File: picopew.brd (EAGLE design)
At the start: 48.4 x 20 mm, 73 parts, among them U1 IS31FL3733-TQLS4

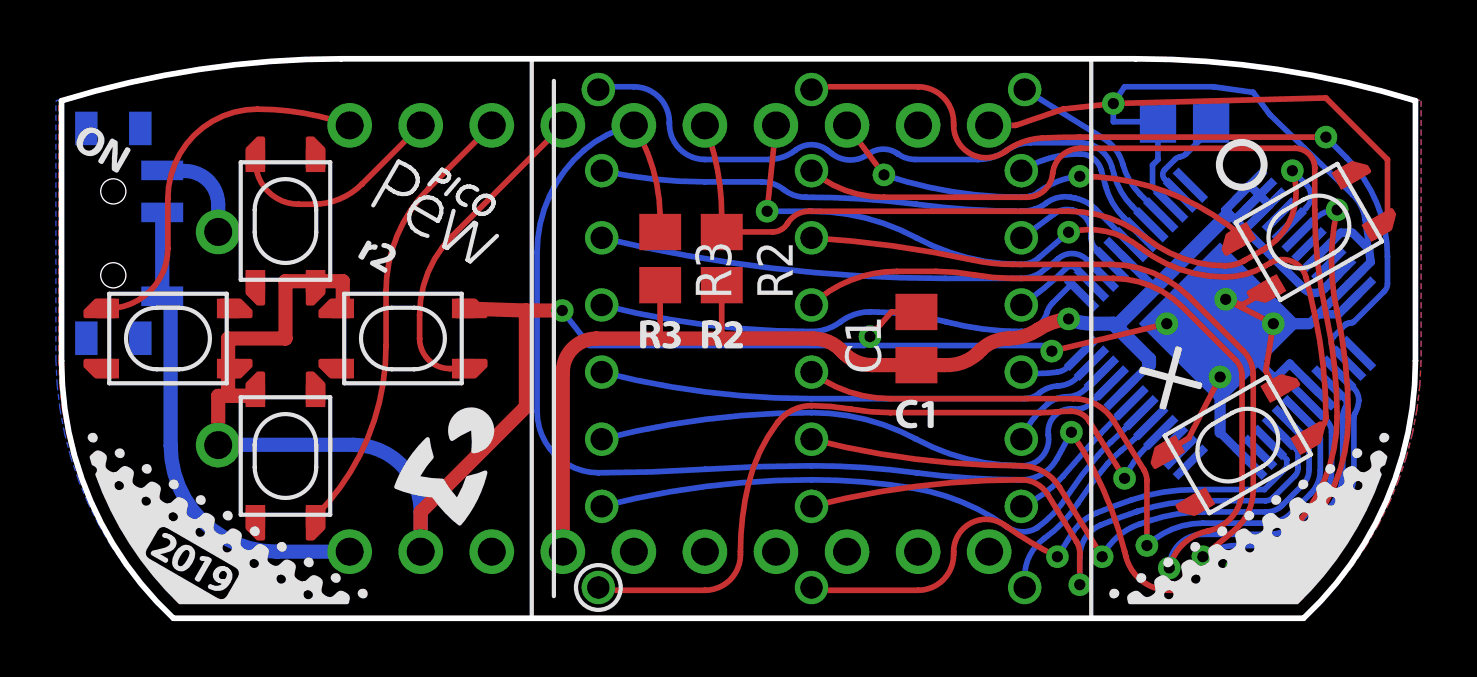
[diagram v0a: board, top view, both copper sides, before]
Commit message: Add JST connector footprint for those who want to connect their battery that way.
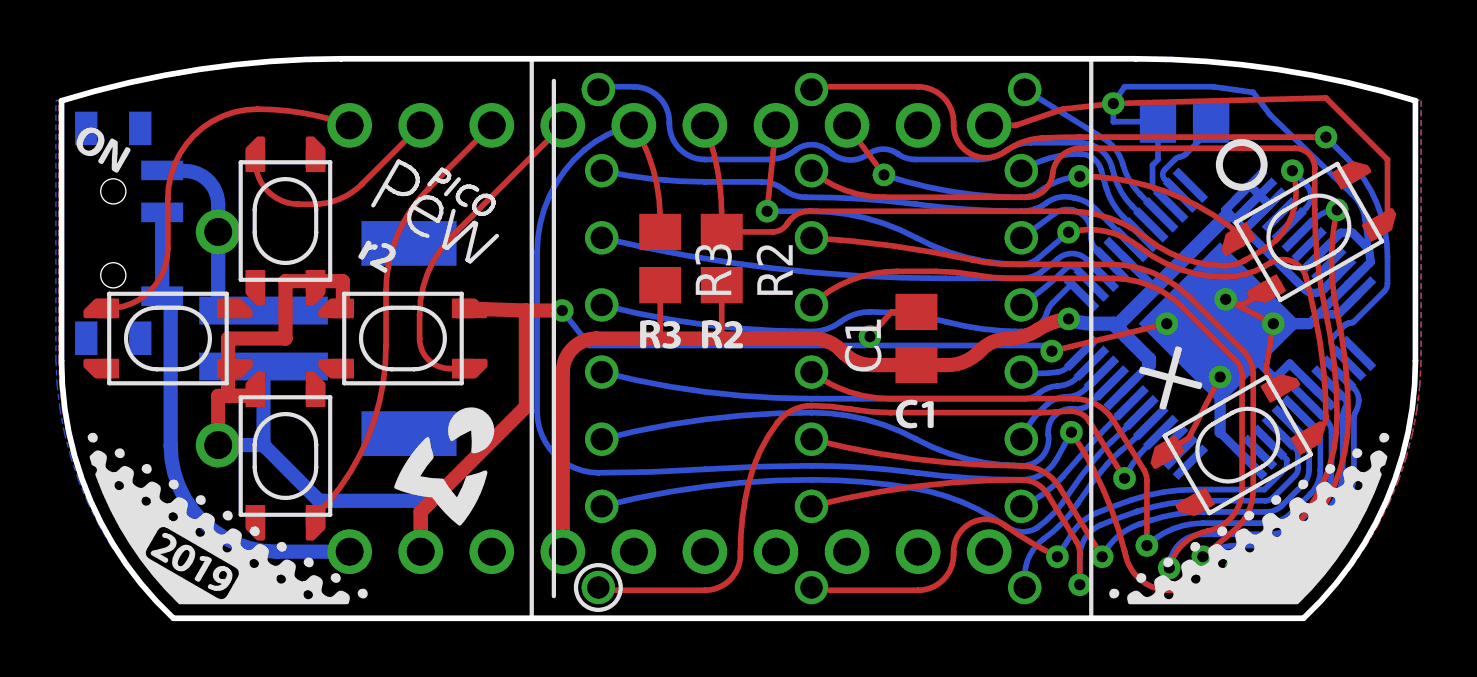
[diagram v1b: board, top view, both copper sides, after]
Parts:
- added CN1: (no value), cwpackage:JST-PH-2-SMT-RA
- moved U$12 1.28 mm to (7.00, 7.40)
- moved U$4 1.28 mm to (7.00, 12.6)
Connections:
- net GND: now also CN1.2
- net N$31: now also CN1.1
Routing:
- net N$31: track 2.88 -> 7.91 mm
- net GND: track 138.5 -> 141.6 mm
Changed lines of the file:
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@@
 <element name="U$30" library="cwtypeset" package="CHAR054" value="" x="20" y="6.857" rot="MR270"/>
 <element name="U$31" library="cwtypeset" package="CHAR057" value="" x="20" y="6.092" rot="MR270"/>
-<element name="U$4" library="cwlogo" package="PLUS" value="" x="8" y="11.8" rot="MR270"/>
-<element name="U$12" library="cwlogo" package="MINUS" value="" x="8" y="8.2" rot="MR270"/>
+<element name="U$4" library="cwlogo" package="PLUS" value="" x="7" y="12.6" rot="MR270"/>
+<element name="U$12" library="cwlogo" package="MINUS" value="" x="7" y="7.4" rot="MR270"/>
+<element name="CN1" library="cwpackage" package="JST-PH-2-SMT-RA" value="" x="13.32" y="10" rot="MR90"/>
 </elements>
 <signals>
@@
 <wire x1="47.6" y1="18.6" x2="49.8" y2="16.4" width="0.2032" layer="1"/>
 <wire x1="49.8" y1="16.4" x2="49.8" y2="14.36456875" width="0.2032" layer="1"/>
-<wire x1="15.24" y1="2.38" x2="15.24" y2="3.8" width="0.508" layer="16"/>
-<wire x1="15.24" y1="3.8" x2="12.84" y2="6.2" width="0.508" layer="16" curve="90"/>
-<wire x1="8" y1="6.2" x2="12.84" y2="6.2" width="0.508" layer="16"/>
+<wire x1="15.24" y1="2.38" x2="15.24" y2="4.2" width="0.508" layer="16"/>
 <wire x1="41.595" y1="17.75" x2="40" y2="17.75" width="0.2032" layer="16"/>
 <wire x1="40" y1="17.75" x2="40" y2="18.4" width="0.2032" layer="16"/>
@@
 <wire x1="48.125940625" y1="13.780278125" x2="48.550203125" y2="13.780278125" width="0.3048" layer="16"/>
 <wire x1="48.550203125" y1="13.780278125" x2="49.138675" y2="13.191803125" width="0.3048" layer="16"/>
+<contactref element="CN1" pad="2"/>
+<wire x1="9.62" y1="9" x2="9.62" y2="6.19" width="0.508" layer="16"/>
+<wire x1="9.62" y1="6.19" x2="8" y2="6.19" width="0.508" layer="16"/>
+<wire x1="15.24" y1="4.2" x2="11.6" y2="4.2" width="0.508" layer="16"/>
+<wire x1="11.6" y1="4.2" x2="9.62" y2="6.19" width="0.508" layer="16"/>
 </signal>
 <signal name="N$1">
@@
 <wire x1="6.8" y1="15.99" x2="8" y2="14.79" width="0.508" layer="16" curve="-90"/>
 <wire x1="8" y1="14.79" x2="8" y2="13.81" width="0.508" layer="16"/>
-<wire x1="6.6" y1="15.99" x2="6" y2="16.01" width="0" layer="19" extent="16-16"/>
+<contactref element="CN1" pad="1"/>
+<wire x1="8" y1="13.81" x2="8" y2="11" width="0.508" layer="16"/>
+<wire x1="8" y1="11" x2="9.62" y2="11" width="0.508" layer="16"/>
+<wire x1="6.6" y1="15.99" x2="6" y2="16.01" width="0.508" layer="16"/>
 </signal>
 <signal name="N$33">

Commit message: Move R2 and R3 to be more centered under the LED matrix.
Hoping this reduces the likelihood that the resistors will prevent the matrix from sitting flush on the board.
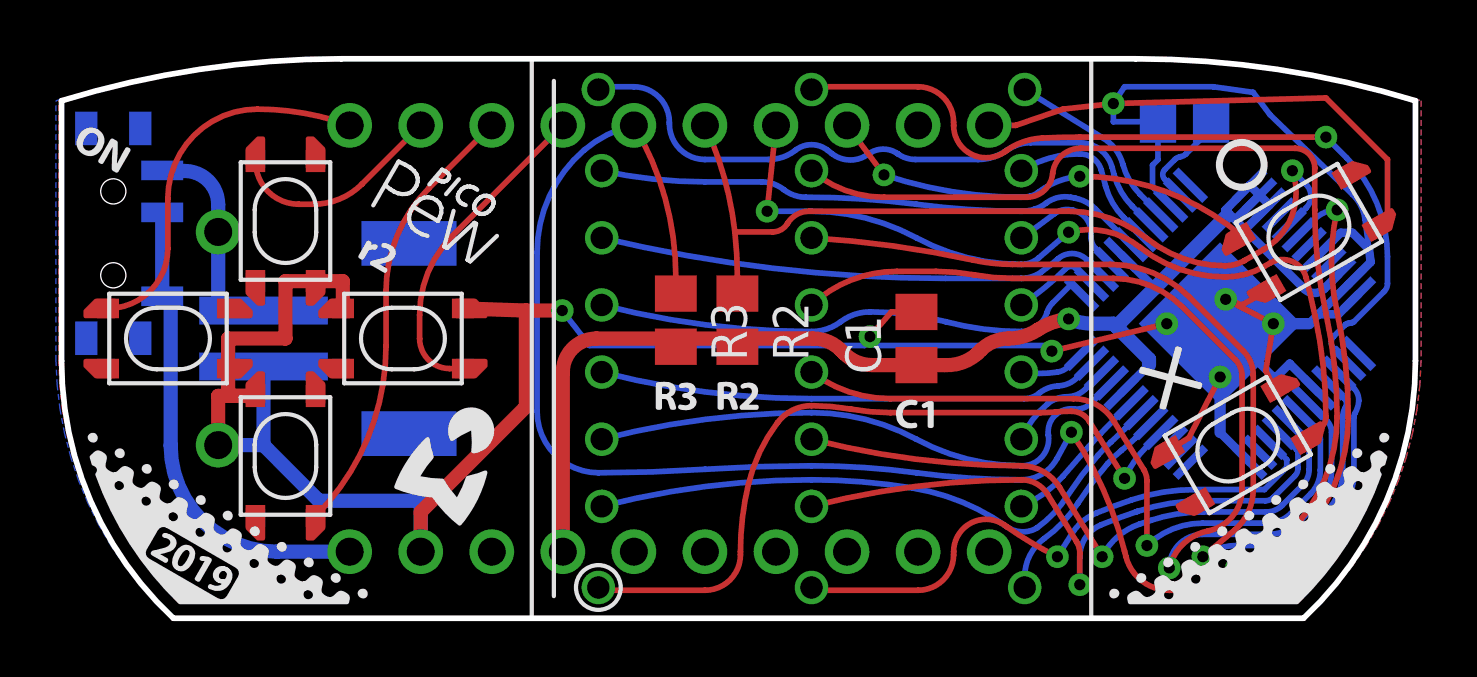
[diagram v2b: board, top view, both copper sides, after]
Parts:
- moved U$20 2.27 mm to (25.8, 7.45)
- moved U$21 2.27 mm to (26.6, 7.45)
- moved U$22 2.27 mm to (23.6, 7.45)
- moved U$23 2.27 mm to (24.4, 7.45)
- moved R2 2.27 mm to (26.6, 10.7)
- moved R3 2.27 mm to (24.4, 10.7)
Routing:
- net +3V3: track 52.0 -> 48.8 mm
- net N$26: track 62.3 -> 64.6 mm
- net N$25: track 29.3 -> 31.1 mm
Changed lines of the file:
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@@
 <element name="X" library="cwpackage" package="MICROPUSHBUTTON" value="PTS815" x="44.45" y="6.19" rot="R30"/>
 <element name="R1" library="resistor" package="R0805" value="22K" x="42.545" y="17.75" rot="MR180"/>
-<element name="R2" library="resistor" package="R0805" value="4.7K" x="26" y="12.8575" rot="R270"/>
-<element name="R3" library="resistor" package="R0805" value="4.7K" x="23.8" y="12.8575" rot="R270"/>
+<element name="R2" library="resistor" package="R0805" value="4.7K" x="26.56" y="10.6575" rot="R270"/>
+<element name="R3" library="resistor" package="R0805" value="4.7K" x="24.36" y="10.6575" rot="R270"/>
 <element name="C1" library="resistor" package="C0805" value="1µ" x="32.96" y="10" rot="R90"/>
 <element name="3" library="cwpackage" package="MICROSLIDESWITCH" value="PCM12SMTR" x="4.25" y="13.76" rot="MR90"/>
@@
 <element name="U$14" library="cwtypeset" package="CHAR082" value="" x="45.75" y="18.45" rot="MR270"/>
 <element name="U$19" library="cwtypeset" package="CHAR049" value="" x="45.75" y="17.625" rot="MR270"/>
-<element name="U$20" library="cwtypeset" package="CHAR082" value="" x="25.24" y="9.65"/>
-<element name="U$21" library="cwtypeset" package="CHAR050" value="" x="26.065" y="9.65"/>
-<element name="U$22" library="cwtypeset" package="CHAR082" value="" x="23.03" y="9.65"/>
-<element name="U$23" library="cwtypeset" package="CHAR051" value="" x="23.855" y="9.65"/>
+<element name="U$20" library="cwtypeset" package="CHAR082" value="" x="25.8" y="7.45"/>
+<element name="U$21" library="cwtypeset" package="CHAR050" value="" x="26.625" y="7.45"/>
+<element name="U$22" library="cwtypeset" package="CHAR082" value="" x="23.59" y="7.45"/>
+<element name="U$23" library="cwtypeset" package="CHAR051" value="" x="24.415" y="7.45"/>
 <element name="U$24" library="cwtypeset" package="CHAR067" value="" x="32.22" y="6.8"/>
 <element name="U$25" library="cwtypeset" package="CHAR049" value="" x="33.059" y="6.8"/>
@@
 <wire x1="28.35189375" y1="14.1135125" x2="29.121775" y2="14.55" width="0.2032" layer="1" curve="-59.102503"/>
 <wire x1="29.121775" y1="14.55" x2="38.4" y2="14.55" width="0.2032" layer="1"/>
-<wire x1="26.0375" y1="13.81" x2="27.816553125" y2="13.81" width="0.2032" layer="1"/>
-<wire x1="27.816553125" y1="13.81" x2="28.35189375" y2="14.1135125" width="0.2032" layer="1" curve="59.102542"/>
-<wire x1="26.0375" y1="13.81" x2="26" y2="13.8075" width="0.2032" layer="1"/>
 <wire x1="44" y1="12.6" x2="44.675209375" y2="12.780921875" width="0.2032" layer="1" curve="29.999803"/>
 <wire x1="44.675209375" y1="12.780921875" x2="44.68268125" y2="12.785234375" width="0.2032" layer="1"/>
-<wire x1="26" y1="13.8075" x2="26" y2="14.4" width="0.2032" layer="1"/>
-<wire x1="26" y1="14.4" x2="25.4" y2="17.62" width="0.2032" layer="1" curve="21.11036"/>
 <wire x1="44.68268125" y1="12.785234375" x2="45.353453125" y2="13.172503125" width="0.2032" layer="1"/>
 <wire x1="45.353453125" y1="13.172503125" x2="46.4" y2="16" width="0.2032" layer="1" curve="79.378049"/>
 <wire x1="38.4" y1="14.55" x2="41.2" y2="13.575" width="0.2032" layer="1" curve="-38.397747"/>
 <wire x1="41.2" y1="13.575" x2="44" y2="12.6" width="0.2032" layer="1" curve="38.39785"/>
+<wire x1="26.56" y1="11.6075" x2="26.56" y2="12.2" width="0.2032" layer="1"/>
+<wire x1="27.816553125" y1="13.81" x2="28.35189375" y2="14.1135125" width="0.2032" layer="1" curve="59.102542"/>
+<wire x1="26.56" y1="12.2" x2="26.47" y2="13.81" width="0.2032" layer="1" curve="6.399079"/>
+<wire x1="26.47" y1="13.81" x2="25.4" y2="17.62" width="0.2032" layer="1" curve="18.575561"/>
+<wire x1="26.47" y1="13.81" x2="27.816553125" y2="13.81" width="0.2032" layer="1"/>
 </signal>
 <signal name="N$26">
@@
 <wire x1="21.08011875" y1="16.73410625" x2="19.4" y2="13.07873125" width="0.2032" layer="16" curve="49.369807"/>
 <wire x1="19.4" y1="13.07873125" x2="19.4" y2="7.4" width="0.2032" layer="16"/>
-<wire x1="23.8" y1="13.8075" x2="23.8" y2="14.4" width="0.2032" layer="1"/>
-<wire x1="23.8" y1="14.4" x2="22.86" y2="17.62" width="0.2032" layer="1" curve="30.13056"/>
 <wire x1="46.48615625" y1="2.6988625" x2="44.955028125" y2="1.223853125" width="0.2032" layer="1"/>
 <wire x1="48.4" y1="7.2" x2="46.48615625" y2="2.6988625" width="0.2032" layer="1" curve="-46.069537"/>
@@
 <wire x1="38.5" y1="6.65" x2="37.98606875" y2="5.70759375" width="0.2032" layer="16"/>
 <wire x1="37.98606875" y1="5.70759375" x2="36.71" y2="4.95" width="0.2032" layer="16" curve="-61.394623"/>
+<wire x1="24.36" y1="11.6075" x2="24.36" y2="12.2" width="0.2032" layer="1"/>
+<wire x1="24.36" y1="12.2" x2="22.86" y2="17.62" width="0.2032" layer="1" curve="30.939147"/>
 </signal>
 <signal name="+3V3">
@@
 <wire x1="20.32" y1="2.38" x2="20.32" y2="8.8" width="0.508" layer="1"/>
 <wire x1="20.32" y1="8.8" x2="21.52" y2="10" width="0.508" layer="1" curve="-90"/>
-<wire x1="21.52" y1="10" x2="23.8" y2="10" width="0.508" layer="1"/>
-<wire x1="23.8" y1="10" x2="26" y2="10" width="0.508" layer="1"/>
 <via x="38.4" y="10.7" extent="1-16" drill="0.4" diameter="0.8128"/>
-<wire x1="26" y1="11.9075" x2="26" y2="10" width="0.2032" layer="1"/>
-<wire x1="23.8" y1="11.9075" x2="23.8" y2="10" width="0.2032" layer="1"/>
-<wire x1="26" y1="10" x2="29.2651" y2="10" width="0.508" layer="1"/>
 <wire x1="29.2651" y1="10" x2="30.25505" y2="9.58995" width="0.508" layer="1" curve="-45"/>
 <wire x1="30.25505" y1="9.58995" x2="30.38495" y2="9.46005" width="0.508" layer="1"/>
@@
 <wire x1="39.273415625" y1="10.53" x2="40.005" y2="10.53" width="0.508" layer="16"/>
 <wire x1="40.005" y1="10.53" x2="40.105" y2="10.43" width="0.508" layer="16"/>
+<wire x1="29.2651" y1="10" x2="26.56" y2="10" width="0.508" layer="1"/>
+<wire x1="21.52" y1="10" x2="24.36" y2="10" width="0.508" layer="1"/>
+<wire x1="24.36" y1="9.7075" x2="24.36" y2="10" width="0.2032" layer="1"/>
+<wire x1="24.36" y1="10" x2="26.56" y2="10" width="0.508" layer="1"/>
+<wire x1="26.56" y1="10" x2="26.56" y2="9.7075" width="0.2032" layer="1"/>
 </signal>
 <signal name="N$27">
